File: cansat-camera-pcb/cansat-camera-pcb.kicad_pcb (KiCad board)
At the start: 8 copper layers, 50 x 50 mm, 63 parts, among them IC2 TLV74315PDBVR, J1 Conn_01x08_Pin, J2 Micro_SD_Card_Det2, J4 Conn_02x10_Odd_Even, J5 Conn_02x10_Odd_Even, J6 OV5640, SW2 SW_Push, U1 IS42S16800F-5TLI, U2 AP2112K-3.3, U4 STM32H743ZITx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

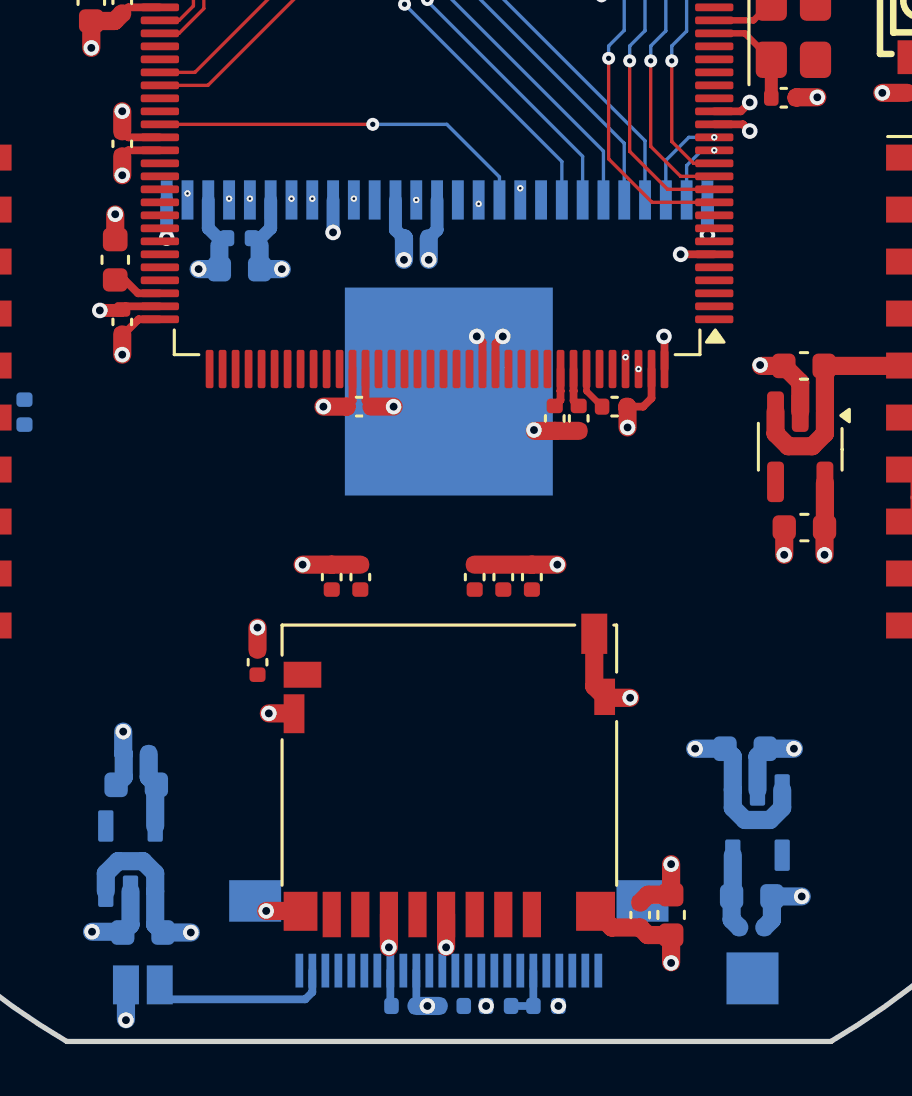
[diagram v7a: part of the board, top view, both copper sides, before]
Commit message: new sdram added, some routing
sdram added to both footprint library and symbol library
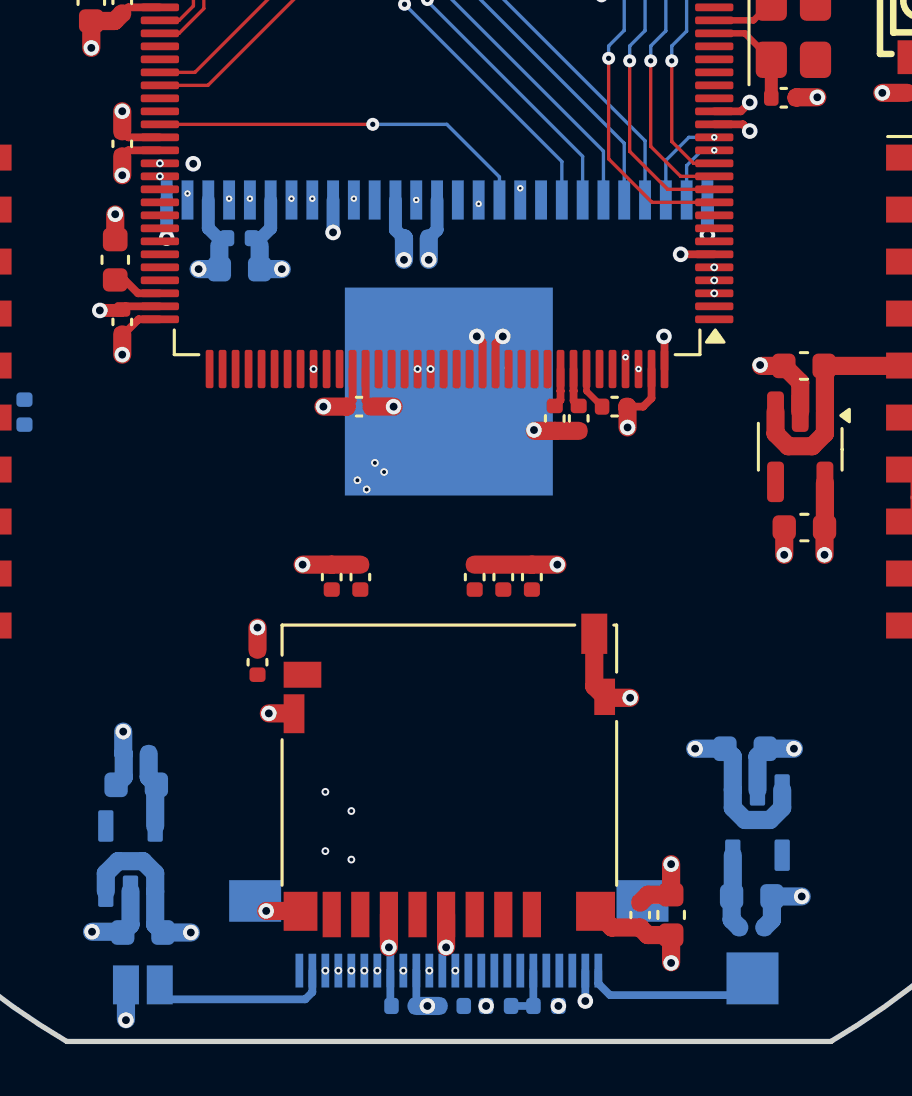
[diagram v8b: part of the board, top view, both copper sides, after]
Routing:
- net /DCMI_D4: track 0.00 -> 36.3 mm, vias 0 -> 2
- net /DCMI_D0: track 0.00 -> 34.5 mm, vias 0 -> 2
- net /DCMI_D6: track 0.00 -> 33.8 mm, vias 0 -> 2
- net /DCMI_D1: track 0.00 -> 33.4 mm, vias 0 -> 2
- net /DCMI_D7: track 0.00 -> 32.8 mm, vias 0 -> 2
- net /DCMI_D2: track 0.00 -> 24.6 mm, vias 0 -> 6
- net /DCMI_D5: track 0.00 -> 24.6 mm, vias 0 -> 2
- net /DCMI_D3: track 0.00 -> 24.4 mm, vias 0 -> 6
- net /camera/STROBE: track 0.00 -> 6.88 mm
- net GND: track 87.7 -> 88.9 mm, vias 45 -> 46
- net +3.3V: vias 32 -> 33
